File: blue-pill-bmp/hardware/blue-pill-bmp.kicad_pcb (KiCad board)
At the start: 2 copper layers, 58.5 x 19.8 mm, 36 parts, among them J2 USB_C_16PIN, J3 Conn_01x04, J4 Conn_02x05_SWD, SW1 SW_SPST, SW2 SW_DPDT_x2, U1 STM32F103C8T6, X1 8MHz, X2 32.768kHz

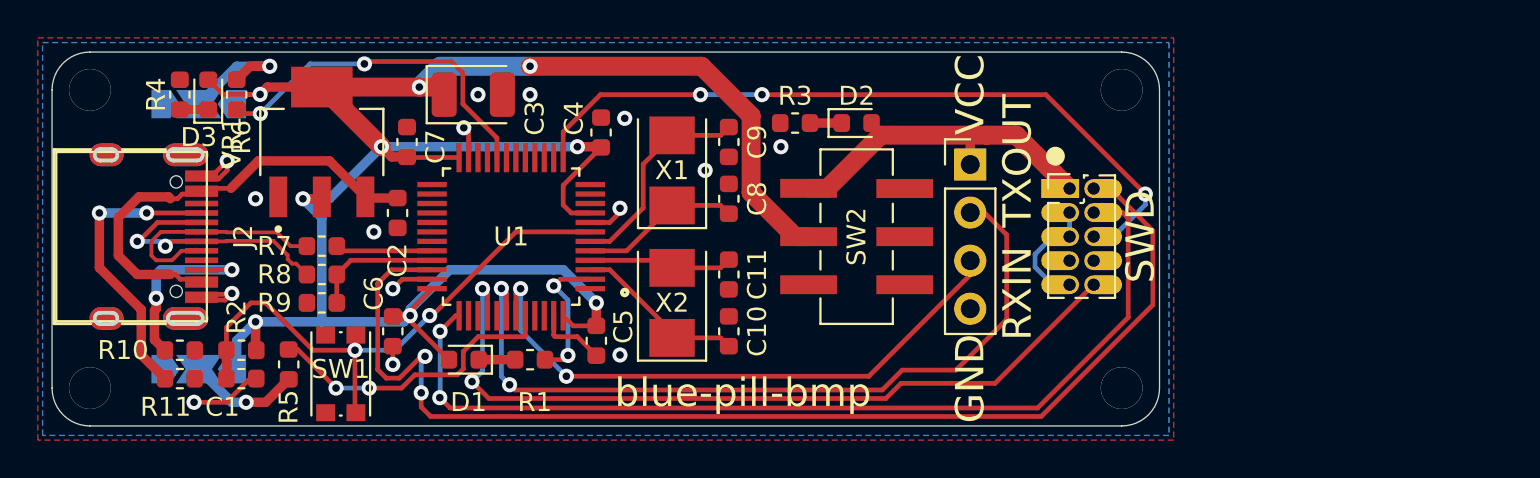
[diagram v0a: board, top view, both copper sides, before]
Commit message: blue-pill-bmp: add 2.54mm SWD connector
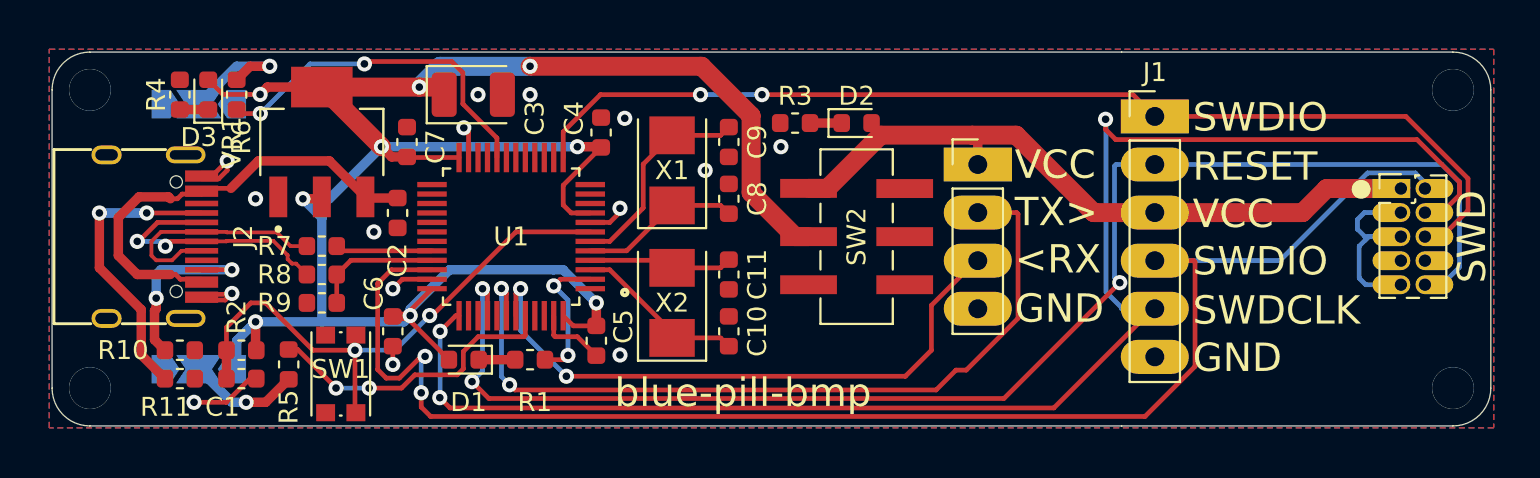
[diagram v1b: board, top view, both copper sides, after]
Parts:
- added J1: Conn_01x06, tom-connectors:PinHeader_1x06_P2.54mm_Vertical, F.Cu at (153.5, 93.7)
- moved J4 17.5 mm to (166.5, 97.5)
- moved J3 0.40 mm to (144.2, 96.2)
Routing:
- net /PB4: track 42.4 -> 75.4 mm, vias 2 -> 3
- net /SWDCLK: track 50.6 -> 82.1 mm, vias 2 -> 3
- net /VTARGET: track 18.7 -> 37.2 mm
- net /SWDIO: track 62.9 -> 80.2 mm
- net /PA3: track 39.1 -> 56.3 mm, vias 3 -> 2
- net GND: track 27.8 -> 33.6 mm
- net /PB6: track 40.9 -> 43.0 mm
- net /PB7: track 31.8 -> 32.8 mm
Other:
- board size 58.5 x 19.8 mm -> 76 x 19.8 mm
- rule pad_to_mask_clearance: 0.05 -> 0
- board text added: "1"
- board text added: "<RX"
- board text added: "O"
- board text added: "RESET"
- board text added: "SWDCLK"
- board text added: "SWDIO"
- board text added: "TX>"
- board text removed: "RXIN"
- board text removed: "TXOUT"
